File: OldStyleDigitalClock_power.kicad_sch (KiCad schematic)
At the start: 24 parts, among them J1 USB_A_OUT, J2 USB_A_OUT, J3 USB_C_IN, U12 NE555D

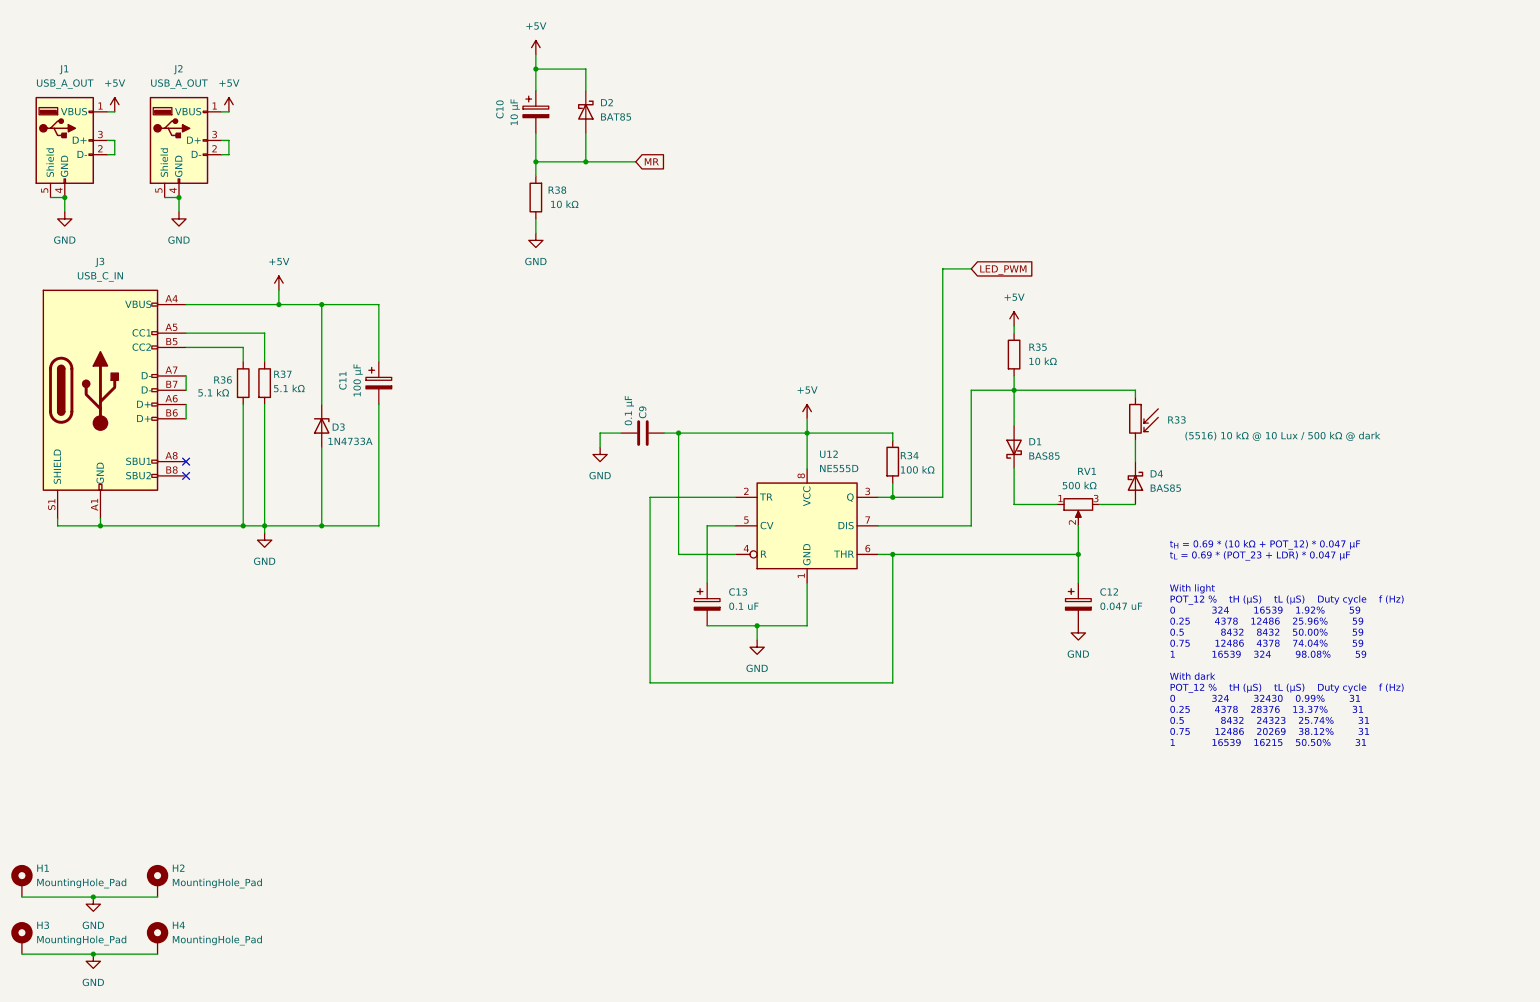
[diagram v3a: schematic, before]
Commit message: pcb rough organisation
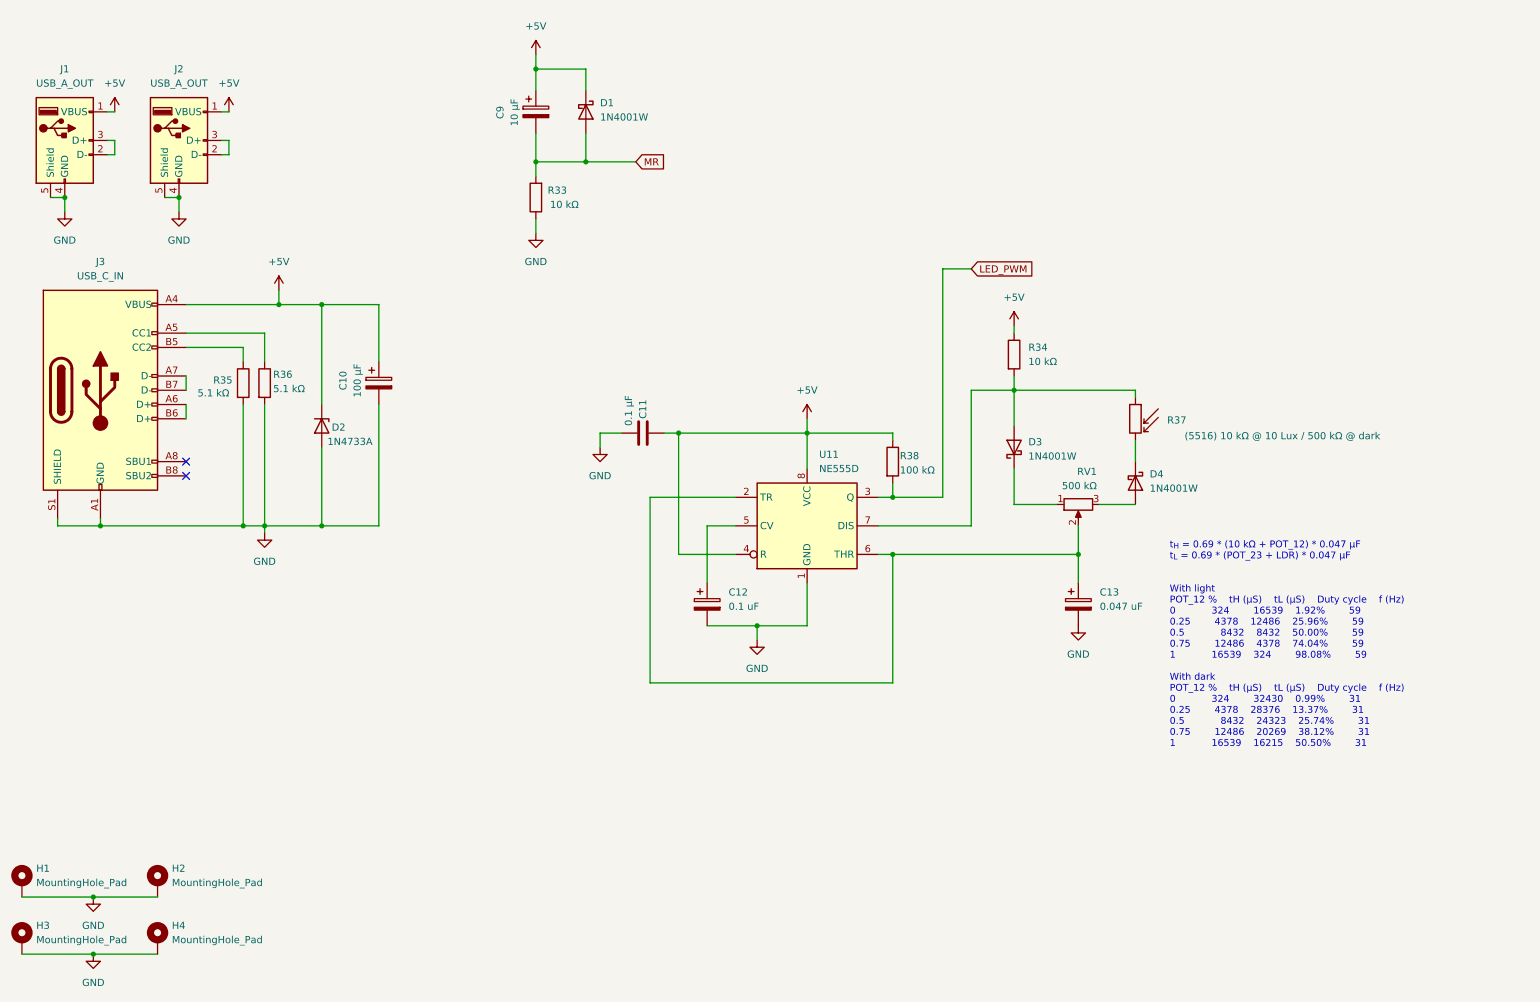
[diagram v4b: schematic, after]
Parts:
- D1: renamed from D2; value BAT85 -> 1N4001W; footprint Diode_THT:D_DO-35_SOD27_P7.62mm_Horizontal -> Diode_SMD:D_SOD-123
- D2: renamed from D3; footprint Diode_THT:D_DO-35_SOD27_P7.62mm_Horizontal -> Diode_SMD:D_SOD-123
- D3: renamed from D1; value BAS85 -> 1N4001W; footprint Diode_THT:D_DO-35_SOD27_P7.62mm_Horizontal -> Diode_SMD:D_SOD-123
- D4: value BAS85 -> 1N4001W; footprint Diode_THT:D_DO-35_SOD27_P7.62mm_Horizontal -> Diode_SMD:D_SOD-123
- renumbered C11 to C10, C9 to C11, C13 to C12, C12 to C13, C10 to C9, R38 to R33, R35 to R34, R36 to R35, R37 to R36, R33 to R37, R34 to R38, U12 to U11
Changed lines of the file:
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@@
 		(on_board yes)
 		(dnp no)
-		(property "Reference" "R36"
+		(property "Reference" "R35"
 			(at 59.436 83.312 0)
 			(effects
@@
 			(project "OldStyleDigitalClock"
 				(path "/a24f1d5b-eb61-47a3-9a92-6515e74f7a21/31b03831-3d01-49ef-8f86-173fa6c5d953"
-					(reference "R36")
+					(reference "R35")
 					(unit 1)
 				)
@@
 		(on_board yes)
 		(dnp no)
-		(property "Reference" "#PWR045"
+		(property "Reference" "#PWR044"
 			(at 38.1 191.77 0)
 			(effects
@@
 			(project "OldStyleDigitalClock"
 				(path "/a24f1d5b-eb61-47a3-9a92-6515e74f7a21/31b03831-3d01-49ef-8f86-173fa6c5d953"
-					(reference "#PWR045")
+					(reference "#PWR044")
 					(unit 1)
 				)
@@
 		(dnp no)
 		(fields_autoplaced yes)
-		(property "Reference" "C12"
+		(property "Reference" "C13"
 			(at 217.17 121.0309 0)
 			(effects
@@
 			(project "OldStyleDigitalClock"
 				(path "/a24f1d5b-eb61-47a3-9a92-6515e74f7a21/31b03831-3d01-49ef-8f86-173fa6c5d953"
-					(reference "C12")
+					(reference "C13")
 					(unit 1)
 				)
@@
 		(on_board yes)
 		(dnp no)
-		(property "Reference" "#PWR044"
+		(property "Reference" "#PWR043"
 			(at 38.1 181.61 0)
 			(effects
@@
 			(project "OldStyleDigitalClock"
 				(path "/a24f1d5b-eb61-47a3-9a92-6515e74f7a21/31b03831-3d01-49ef-8f86-173fa6c5d953"
-					(reference "#PWR044")
+					(reference "#PWR043")
 					(unit 1)
 				)
@@
 		(dnp no)
 		(fields_autoplaced yes)
-		(property "Reference" "R35"
+		(property "Reference" "R34"
 			(at 204.47 77.4699 0)
 			(effects
@@
 			(project "OldStyleDigitalClock"
 				(path "/a24f1d5b-eb61-47a3-9a92-6515e74f7a21/31b03831-3d01-49ef-8f86-173fa6c5d953"
-					(reference "R35")
+					(reference "R34")
 					(unit 1)
 				)
@@
 		(on_board yes)
 		(dnp no)
-		(property "Reference" "#PWR030"
+		(property "Reference" "#PWR037"
 			(at 201.93 77.47 0)
 			(effects
@@
 			(project "OldStyleDigitalClock"
 				(path "/a24f1d5b-eb61-47a3-9a92-6515e74f7a21/31b03831-3d01-49ef-8f86-173fa6c5d953"
-					(reference "#PWR030")
+					(reference "#PWR037")
 					(unit 1)
 				)
@@
 		(dnp no)
 		(fields_autoplaced yes)
-		(property "Reference" "C13"
+		(property "Reference" "C12"
 			(at 151.13 121.0309 0)
 			(effects
@@
 			(project "OldStyleDigitalClock"
 				(path "/a24f1d5b-eb61-47a3-9a92-6515e74f7a21/31b03831-3d01-49ef-8f86-173fa6c5d953"
-					(reference "C13")
+					(reference "C12")
 					(unit 1)
 				)
@@
 		(dnp no)
 		(fields_autoplaced yes)
-		(property "Reference" "D2"
+		(property "Reference" "D1"
 			(at 128.27 33.9724 90)
 			(effects
@@
 			)
 		)
-		(property "Value" "BAT85"
+		(property "Value" "1N4001W"
 			(at 128.27 36.5124 90)
 			(effects
@@
 			)
 		)
-		(property "Footprint" "Diode_THT:D_DO-35_SOD27_P7.62mm_Horizontal"
+		(property "Footprint" "Diode_SMD:D_SOD-123"
 			(at 121.285 35.56 0)
 			(effects
@@
 			(project "OldStyleDigitalClock"
 				(path "/a24f1d5b-eb61-47a3-9a92-6515e74f7a21/31b03831-3d01-49ef-8f86-173fa6c5d953"
-					(reference "D2")
+					(reference "D1")
 					(unit 1)
 				)
@@
 		(on_board yes)
 		(dnp no)
-		(property "Reference" "R34"
+		(property "Reference" "R38"
 			(at 181.61 96.774 0)
 			(effects
@@
 			(project "OldStyleDigitalClock"
 				(path "/a24f1d5b-eb61-47a3-9a92-6515e74f7a21/31b03831-3d01-49ef-8f86-173fa6c5d953"
-					(reference "R34")
+					(reference "R38")
 					(unit 1)
 				)
@@
 		(on_board yes)
 		(dnp no)
-		(property "Reference" "D3"
+		(property "Reference" "D2"
 			(at 80.518 91.694 90)
 			(effects
@@
 			)
 		)
-		(property "Footprint" "Diode_THT:D_DO-35_SOD27_P7.62mm_Horizontal"
+		(property "Footprint" "Diode_SMD:D_SOD-123"
 			(at 78.74 91.44 0)
 			(effects
@@
 			(project "OldStyleDigitalClock"
 				(path "/a24f1d5b-eb61-47a3-9a92-6515e74f7a21/31b03831-3d01-49ef-8f86-173fa6c5d953"
-					(reference "D3")
+					(reference "D2")
 					(unit 1)
 				)
@@
 		(on_board yes)
 		(dnp no)
-		(property "Reference" "C11"
+		(property "Reference" "C10"
 			(at 82.55 85.09 90)
 			(effects
@@
 			(project "OldStyleDigitalClock"
 				(path "/a24f1d5b-eb61-47a3-9a92-6515e74f7a21/31b03831-3d01-49ef-8f86-173fa6c5d953"
-					(reference "C11")
+					(reference "C10")
 					(unit 1)
 				)
@@
 		(on_board yes)
 		(dnp no)
-		(property "Reference" "R33"
+		(property "Reference" "R37"
 			(at 230.886 90.424 0)
 			(effects
@@
 			(project ""
 				(path "/a24f1d5b-eb61-47a3-9a92-6515e74f7a21/31b03831-3d01-49ef-8f86-173fa6c5d953"
-					(reference "R33")
+					(reference "R37")
 					(unit 1)
 				)
@@
 		(on_board yes)
 		(dnp no)
-		(property "Reference" "#PWR038"
+		(property "Reference" "#PWR030"
 			(at 116.84 29.21 0)
 			(effects
@@
 			(project "OldStyleDigitalClock"
 				(path "/a24f1d5b-eb61-47a3-9a92-6515e74f7a21/31b03831-3d01-49ef-8f86-173fa6c5d953"
-					(reference "#PWR038")
+					(reference "#PWR030")
 					(unit 1)
 				)
@@
 		(on_board yes)
 		(dnp no)
-		(property "Reference" "C9"
+		(property "Reference" "C11"
 			(at 135.89 90.17 0)
 			(effects
@@
 			(project "OldStyleDigitalClock"
 				(path "/a24f1d5b-eb61-47a3-9a92-6515e74f7a21/31b03831-3d01-49ef-8f86-173fa6c5d953"
-					(reference "C9")
+					(reference "C11")
 					(unit 1)
 				)
@@
 		(on_board yes)
 		(dnp no)
-		(property "Reference" "#PWR041"
+		(property "Reference" "#PWR035"
 			(at 116.84 63.5 0)
 			(effects
@@
 			(project "OldStyleDigitalClock"
 				(path "/a24f1d5b-eb61-47a3-9a92-6515e74f7a21/31b03831-3d01-49ef-8f86-173fa6c5d953"
-					(reference "#PWR041")
+					(reference "#PWR035")
 					(unit 1)
 				)
@@
 		(on_board yes)
 		(dnp no)
-		(property "Reference" "C10"
+		(property "Reference" "C9"
 			(at 110.49 36.83 90)
 			(effects
@@
 			(project "OldStyleDigitalClock"
 				(path "/a24f1d5b-eb61-47a3-9a92-6515e74f7a21/31b03831-3d01-49ef-8f86-173fa6c5d953"
-					(reference "C10")
+					(reference "C9")
 					(unit 1)
 				)
@@
 		(dnp no)
 		(fields_autoplaced yes)
-		(property "Reference" "#PWR043"
+		(property "Reference" "#PWR040"
 			(at 68.58 116.84 0)
 			(effects
@@
 			(project "OldStyleDigitalClock"
 				(path "/a24f1d5b-eb61-47a3-9a92-6515e74f7a21/31b03831-3d01-49ef-8f86-173fa6c5d953"
-					(reference "#PWR043")
+					(reference "#PWR040")
 					(unit 1)
 				)
@@
 		(on_board yes)
 		(dnp no)
-		(property "Reference" "#PWR035"
+		(property "Reference" "#PWR038"
 			(at 165.1 93.98 0)
 			(effects
@@
 			(project "OldStyleDigitalClock"
 				(path "/a24f1d5b-eb61-47a3-9a92-6515e74f7a21/31b03831-3d01-49ef-8f86-173fa6c5d953"
-					(reference "#PWR035")
+					(reference "#PWR038")
 					(unit 1)
 				)
@@
 		(on_board yes)
 		(dnp no)
-		(property "Reference" "R38"
+		(property "Reference" "R33"
 			(at 120.65 49.53 0)
 			(effects
@@
 			(project "OldStyleDigitalClock"
 				(path "/a24f1d5b-eb61-47a3-9a92-6515e74f7a21/31b03831-3d01-49ef-8f86-173fa6c5d953"
-					(reference "R38")
+					(reference "R33")
 					(unit 1)
 				)
@@
 		(dnp no)
 		(fields_autoplaced yes)
-		(property "Reference" "D1"
+		(property "Reference" "D3"
 			(at 204.47 94.2974 90)
 			(effects
@@
 			)
 		)
-		(property "Value" "BAS85"
+		(property "Value" "1N4001W"
 			(at 204.47 96.8374 90)
 			(effects
@@
 			)
 		)
-		(property "Footprint" "Diode_THT:D_DO-35_SOD27_P7.62mm_Horizontal"
+		(property "Footprint" "Diode_SMD:D_SOD-123"
 			(at 206.375 95.25 0)
 			(effects
@@
 			(project "OldStyleDigitalClock"
 				(path "/a24f1d5b-eb61-47a3-9a92-6515e74f7a21/31b03831-3d01-49ef-8f86-173fa6c5d953"
-					(reference "D1")
+					(reference "D3")
 					(unit 1)
 				)
@@
 		(dnp no)
 		(fields_autoplaced yes)
-		(property "Reference" "U12"
+		(property "Reference" "U11"
 			(at 167.2433 96.52 0)
 			(effects
@@
 			(project ""
 				(path "/a24f1d5b-eb61-47a3-9a92-6515e74f7a21/31b03831-3d01-49ef-8f86-173fa6c5d953"
-					(reference "U12")
+					(reference "U11")
 					(unit 1)
 				)
@@
 		(dnp no)
 		(fields_autoplaced yes)
-		(property "Reference" "#PWR037"
+		(property "Reference" "#PWR039"
 			(at 128.27 101.6 0)
 			(effects
@@
 			(project "OldStyleDigitalClock"
 				(path "/a24f1d5b-eb61-47a3-9a92-6515e74f7a21/31b03831-3d01-49ef-8f86-173fa6c5d953"
-					(reference "#PWR037")
+					(reference "#PWR039")
 					(unit 1)
 				)
@@
 		(dnp no)
 		(fields_autoplaced yes)
-		(property "Reference" "#PWR040"
+		(property "Reference" "#PWR041"
 			(at 213.36 133.35 0)
 			(effects
@@
 			(project "OldStyleDigitalClock"
 				(path "/a24f1d5b-eb61-47a3-9a92-6515e74f7a21/31b03831-3d01-49ef-8f86-173fa6c5d953"
-					(reference "#PWR040")
+					(reference "#PWR041")
 					(unit 1)
 				)
@@
 			)
 		)
-		(property "Value" "BAS85"
+		(property "Value" "1N4001W"
 			(at 226.06 102.5524 90)
 			(effects
@@
 			)
 		)
-		(property "Footprint" "Diode_THT:D_DO-35_SOD27_P7.62mm_Horizontal"
+		(property "Footprint" "Diode_SMD:D_SOD-123"
 			(at 219.075 101.6 0)
 			(effects
@@
 		(on_board yes)
 		(dnp no)
-		(property "Reference" "R37"
+		(property "Reference" "R36"
 			(at 70.104 82.296 0)
 			(effects
@@
 			(project "OldStyleDigitalClock"
 				(path "/a24f1d5b-eb61-47a3-9a92-6515e74f7a21/31b03831-3d01-49ef-8f86-173fa6c5d953"
-					(reference "R37")
-					(unit 1)
-				)
+					(reference "R36")
+					(unit 1)
+				)

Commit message: Tracks 1
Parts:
- removed C12: 0.1 uF, Capacitor_SMD:C_1206_3216Metric, symbol Device:C_Polarized
- added C12: 0.1 µF, Capacitor_SMD:C_1206_3216Metric, symbol Device:C
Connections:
- net GND: now also C12.2
- net at U11.5 (CV): now also C12.1
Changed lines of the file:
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@@
+	)
+	(symbol
+		(lib_id "Device:C")
+		(at 147.32 123.19 0)
+		(mirror y)
+		(unit 1)
+		(exclude_from_sim no)
+		(in_bom yes)
+		(on_board yes)
+		(dnp no)
+		(property "Reference" "C12"
+			(at 144.78 123.19 0)
+			(effects
+				(font
+					(size 1.27 1.27)
+				)
+				(justify left)
+			)
+		)
+		(property "Value" "0.1 µF"
+			(at 146.05 125.73 0)
+			(effects
+				(font
+					(size 1.27 1.27)
+				)
+				(justify left)
+			)
+		)
+		(property "Footprint" "Capacitor_SMD:C_1206_3216Metric"
+			(at 146.3548 127 0)
+			(effects
+				(font
+					(size 1.27 1.27)
+				)
+				(hide yes)
+			)
+		)
+		(property "Datasheet" "~"
+			(at 147.32 123.19 0)
+			(effects
+				(font
+					(size 1.27 1.27)
+				)
+				(hide yes)
+			)
+		)
+		(property "Description" ""
+			(at 147.32 123.19 0)
+			(effects
+				(font
+					(size 1.27 1.27)
+				)
+			)
+		)
+		(pin "1"
+		)
+		(pin "2"
+		)
+		(instances
+			(project "OldStyleDigitalClock"
+				(path "/a24f1d5b-eb61-47a3-9a92-6515e74f7a21/31b03831-3d01-49ef-8f86-173fa6c5d953"
+					(reference "C12")
+					(unit 1)
+				)
+			)
+		)
 	)
 	(symbol
@@
 					(unit 1)
 				)
-			)
-		)
-	)
-	(symbol
-		(lib_id "Device:C_Polarized")
-		(at 147.32 123.19 0)
-		(unit 1)
-		(exclude_from_sim no)
-		(in_bom yes)
-		(on_board yes)
-		(dnp no)
-		(fields_autoplaced yes)
-		(property "Reference" "C12"
-			(at 151.13 121.0309 0)
-			(effects
-				(font
-					(size 1.27 1.27)
-				)
-				(justify left)
-			)
-		)
-		(property "Value" "0.1 uF"
-			(at 151.13 123.5709 0)
-			(effects
-				(font
-					(size 1.27 1.27)
-				)
-				(justify left)
-			)
-		)
-		(property "Footprint" "Capacitor_SMD:C_1206_3216Metric"
-			(at 148.2852 127 0)
-			(effects
-				(font
-					(size 1.27 1.27)
-				)
-				(hide yes)
-			)
-		)
-		(property "Datasheet" "~"
-			(at 147.32 123.19 0)
-			(effects
-				(font
-					(size 1.27 1.27)
-				)
-				(hide yes)
-			)
-		)
-		(property "Description" "Polarized capacitor"
-			(at 147.32 123.19 0)
-			(effects
-				(font
-					(size 1.27 1.27)
-				)
-				(hide yes)
-			)
-		)
-		(pin "1"
-		)
-		(pin "2"
-		)
-		(instances
-			(project "OldStyleDigitalClock"
-				(path "/a24f1d5b-eb61-47a3-9a92-6515e74f7a21/31b03831-3d01-49ef-8f86-173fa6c5d953"
-					(reference "C12")
-					(unit 1)
-				)
